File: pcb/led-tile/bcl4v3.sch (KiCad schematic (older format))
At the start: 36 parts, among them J1 Conn_01x04, J10 Conn_01x04, J2 Conn_01x04, J3 Conn_01x04, J4 Conn_01x04, J5 Conn_01x04, J6 Conn_01x04, J7 Conn_01x04, J8 Conn_01x04, J9 10118194-0001LF, Q1 IRLML6402, U1 STM32F072CBTx, U2 74HC595D_118, U3 TBD62783A, U4 TLC5916ID, U5 MCP1703A-3302_SOT23, Y1 ABS07-120-32.768KHZ-Z

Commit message: pcb: put USB_VBUS to pin header
Replace one pin header with a 5-contact version and route USB_VBUS
to this pin. Necessary to power a plug-on battery shield from the main
USB connector.
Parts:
- removed J3: Conn_01x04, Connector_PinHeader_2.54mm:PinHeader_1x04_P2.54mm_Vertical, symbol Connector_Generic:Conn_01x04
- added J4: Conn_01x05, Connector_PinHeader_2.54mm:PinHeader_1x05_P2.54mm_Vertical, symbol Connector_Generic:Conn_01x05
- LOGO1: symbol bcl4v3-rescue:OSHW-LOGOM-SparkFun-Aesthetics -> bcl4v3-rescue:OSHW-LOGOM-SparkFun-Aesthetics-bcl4v3-rescue-bcl4v3-rescue
- R4: value 680R -> 715R
- renumbered J4 to J3
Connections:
- wire segments 211 -> 212
- no-connect marks 19 -> 17
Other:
- moved on the sheet: J3
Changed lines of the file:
@@
 $Comp
 L Connector_Generic:Conn_01x04 J3
-U 1 1 5BE83443
+U 1 1 5BE834A1
 P 2550 1700
 F 0 "J3" H 2630 1692 50  0000 L CNN
-F 1 "Conn_01x04" H 2630 1601 50  0000 L CNN
+F 1 "Conn_01x04" H 2650 1600 50  0000 L CNN
 F 2 "Connector_PinHeader_2.54mm:PinHeader_1x04_P2.54mm_Vertical" H 2550 1700 50  0001 C CNN
 F 3 "~" H 2550 1700 50  0001 C CNN
 	1    2550 1700
 	1    0    0    -1
-$EndComp
-$Comp
-L Connector_Generic:Conn_01x04 J4
-U 1 1 5BE834A1
-P 2550 2400
-F 0 "J4" H 2630 2392 50  0000 L CNN
-F 1 "Conn_01x04" H 2650 2300 50  0000 L CNN
-F 2 "Connector_PinHeader_2.54mm:PinHeader_1x04_P2.54mm_Vertical" H 2550 2400 50  0001 C CNN
-F 3 "~" H 2550 2400 50  0001 C CNN
-	1    2550 2400
-	1    0    0    1
 $EndComp
 Wire Wire Line
@@
 P 7350 5950
 F 0 "R4" H 7500 6000 50  0000 C CNN
-F 1 "680R" H 7550 5900 50  0000 C CNN
+F 1 "715R" H 7550 5900 50  0000 C CNN
 F 2 "Resistor_SMD:R_0805_2012Metric_Pad1.15x1.40mm_HandSolder" V 7280 5950 50  0001 C CNN
 F 3 "~" H 7350 5950 50  0001 C CNN
@@
 NoConn ~ 4950 2000
 NoConn ~ 4950 2200
-NoConn ~ 4950 2300
-NoConn ~ 4950 2400
 NoConn ~ 4950 2600
 NoConn ~ 4950 2700
@@
 $EndComp
 $Comp
-L bcl4v3-rescue:OSHW-LOGOM-SparkFun-Aesthetics LOGO1
+L bcl4v3-rescue:OSHW-LOGOM-SparkFun-Aesthetics-bcl4v3-rescue-bcl4v3-rescue LOGO1
 U 1 1 5BFECBD9
 P 3750 4450
@@
 Text Label 5050 1150 0    50   ~ 0
 VBAT
+$Comp
+L Connector_Generic:Conn_01x05 J4
+U 1 1 5C7319EC
+P 2550 2300
+F 0 "J4" H 2630 2250 50  0000 L CNN
+F 1 "Conn_01x05" H 2630 2341 50  0000 L CNN
+F 2 "Connector_PinHeader_2.54mm:PinHeader_1x05_P2.54mm_Vertical" H 2550 2300 50  0001 C CNN
+F 3 "~" H 2550 2300 50  0001 C CNN
+	1    2550 2300
+	1    0    0    1
+$EndComp
+Wire Wire Line
+	1750 2100 2350 2100
+Text Label 1750 2100 0    50   ~ 0
+USB_VBUS
 $EndSCHEMATC

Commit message: pcb: update led-tile to latest version
move OSHW logo into a project specific library as not everyone has the
Sparkfun Libraries installed, decrease current through the SMD LED,
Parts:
- LOGO1: footprint Aesthetics:OSHW-LOGO-M -> project:OSHW-LOGO-M; symbol bcl4v3-rescue:OSHW-LOGOM-SparkFun-Aesthetics-bcl4v3-rescue-bcl4v3-rescue -> project:OSHW-LOGOM-SparkFun-Aesthetics
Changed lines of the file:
@@
 $EndComp
 $Comp
-L bcl4v3-rescue:OSHW-LOGOM-SparkFun-Aesthetics-bcl4v3-rescue-bcl4v3-rescue LOGO1
+L project:OSHW-LOGOM-SparkFun-Aesthetics LOGO1
 U 1 1 5BFECBD9
 P 3750 4450
 F 0 "LOGO1" H 3750 4700 45  0001 C CNN
 F 1 "OSHW-LOGOM" H 3750 4050 45  0001 C CNN
-F 2 "Aesthetics:OSHW-LOGO-M" H 3750 4750 20  0001 C CNN
+F 2 "project:OSHW-LOGO-M" H 3750 4750 20  0001 C CNN
 F 3 "" H 3750 4450 50  0001 C CNN
 F 4 "XXX-00000" H 4228 4385 60  0001 L CNN "Field4"

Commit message: pcb: use IS31FL3730 as matrix driver
reduce component count
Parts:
- removed R1: 1k, Resistor_SMD:R_0805_2012Metric_Pad1.15x1.40mm_HandSolder, symbol Device:R
- removed U1: STM32F072CBTx, Package_QFP:LQFP-48_7x7mm_P0.5mm, symbol MCU_ST_STM32F0:STM32F072CBTx
- removed U2: 74HC595D_118, Package_SO:TSSOP-16_4.4x5mm_P0.65mm, symbol dk_Logic-Shift-Registers:74HC595D_118
- removed U3: TBD62783A, Package_SO:SSOP-18_4.4x6.5mm_P0.65mm, symbol Transistor_Array:TBD62783A
- removed U4: TLC5916ID, Package_SO:TSSOP-16_4.4x5mm_P0.65mm, symbol dk_PMIC-LED-Drivers:TLC5916IN
- added C8: 100n, Capacitor_SMD:C_0805_2012Metric_Pad1.15x1.40mm_HandSolder, symbol Device:C_Small
- added JP2, JP3: Jumper_2_Open, project:SMT-JUMPER_2_NC_TRACE_NO-SILK, symbol Jumper:Jumper_2_Open
- added R3, R5: 4k7, Resistor_SMD:R_0805_2012Metric_Pad1.15x1.40mm_HandSolder, symbol Device:R_Small
- added R4: 100k, Resistor_SMD:R_0805_2012Metric_Pad1.15x1.40mm_HandSolder, symbol Device:R_Small
- added U2: STM32F072CBUx, Package_DFN_QFN:QFN-48-1EP_7x7mm_P0.5mm_EP5.6x5.6mm, symbol MCU_ST_STM32F0:STM32F072CBUx
- added U3: IS31FL3730-QFSL2, project:QFN-24-1EP_4x4mm_P0.5mm_EP2.6x2.6mm_ThermalVias, symbol is31fl3730-qfsl2:IS31FL3730-QFSL2
- C6: value 100n -> 1µF
- renumbered C3 to C1, C4 to C2, C5 to C3, C8 to C4, C1 to C5, J8 to J10, J5 to J3, J6 to J4, J9 to J5, J10 to J6, J3 to J7, J4 to J8, J7 to J9, R2 to R1, R4 to R2, U5 to U1
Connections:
- net labels added: MCU_SCL, MCU_SDA, MCU_SDB
- net labels removed: CAT_CLK, CAT_DATA, CAT_STROBE, nOE_COL, nOE_ROW
- wire segments 212 -> 210
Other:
- moved on the sheet: C3, C4

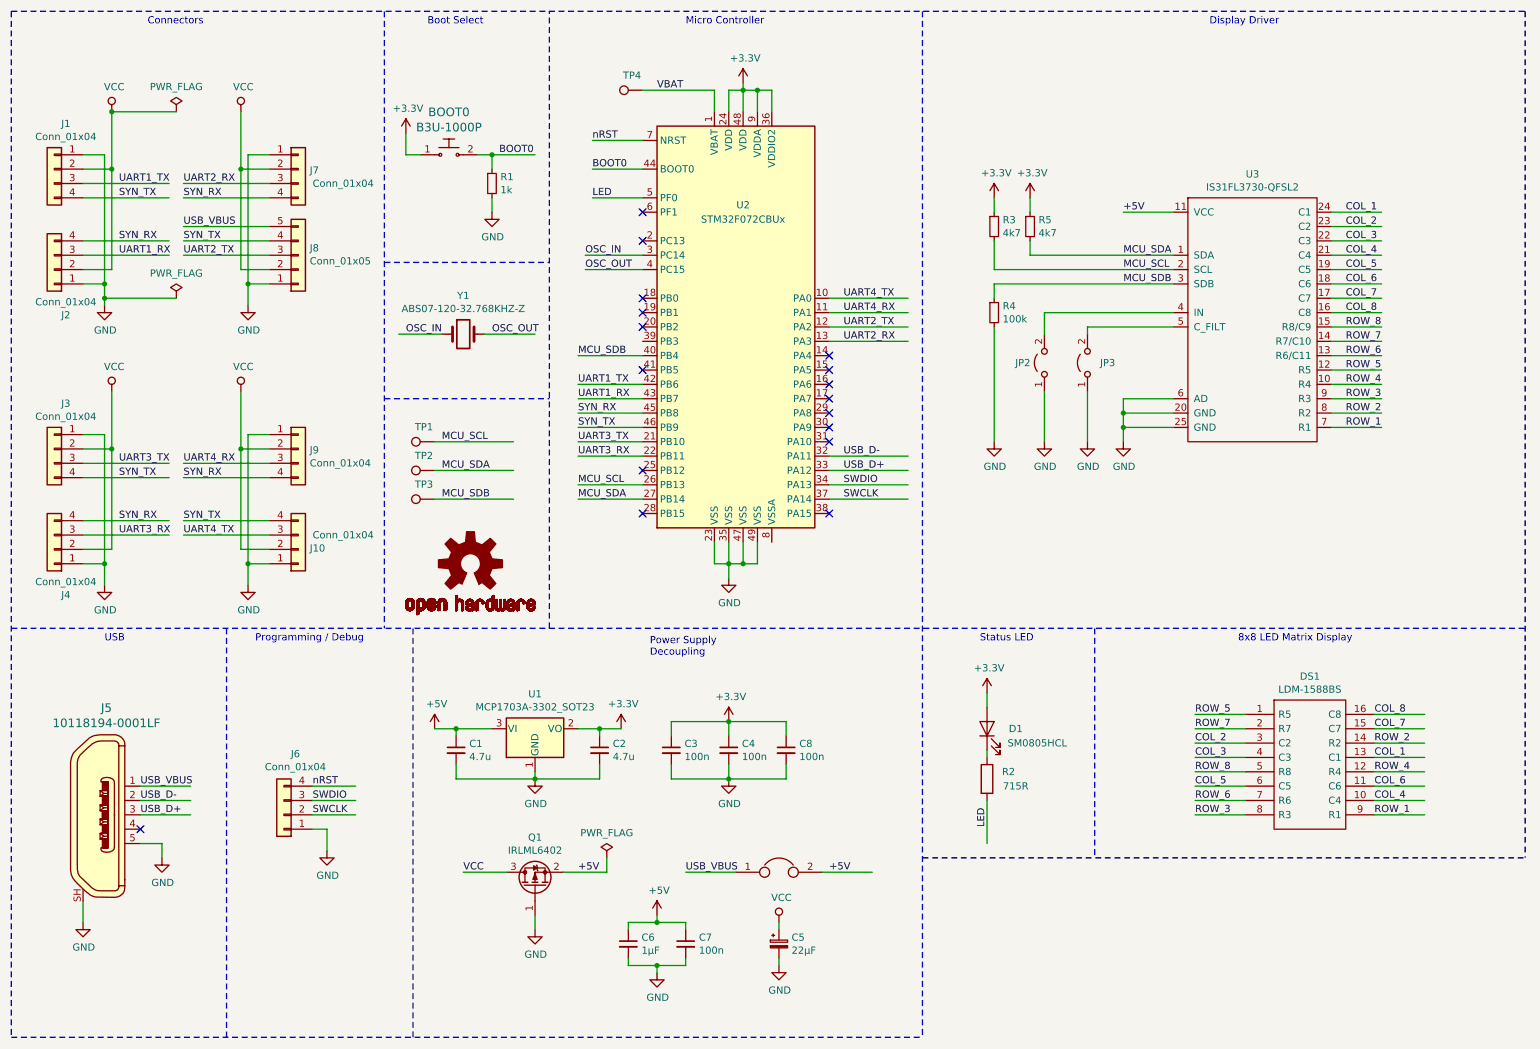
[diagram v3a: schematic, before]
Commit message: Variant of the tile with integrated LED matrix driver
Use ISSI IS31FL3736 instead of discrete ICs for driving the
LED matrix
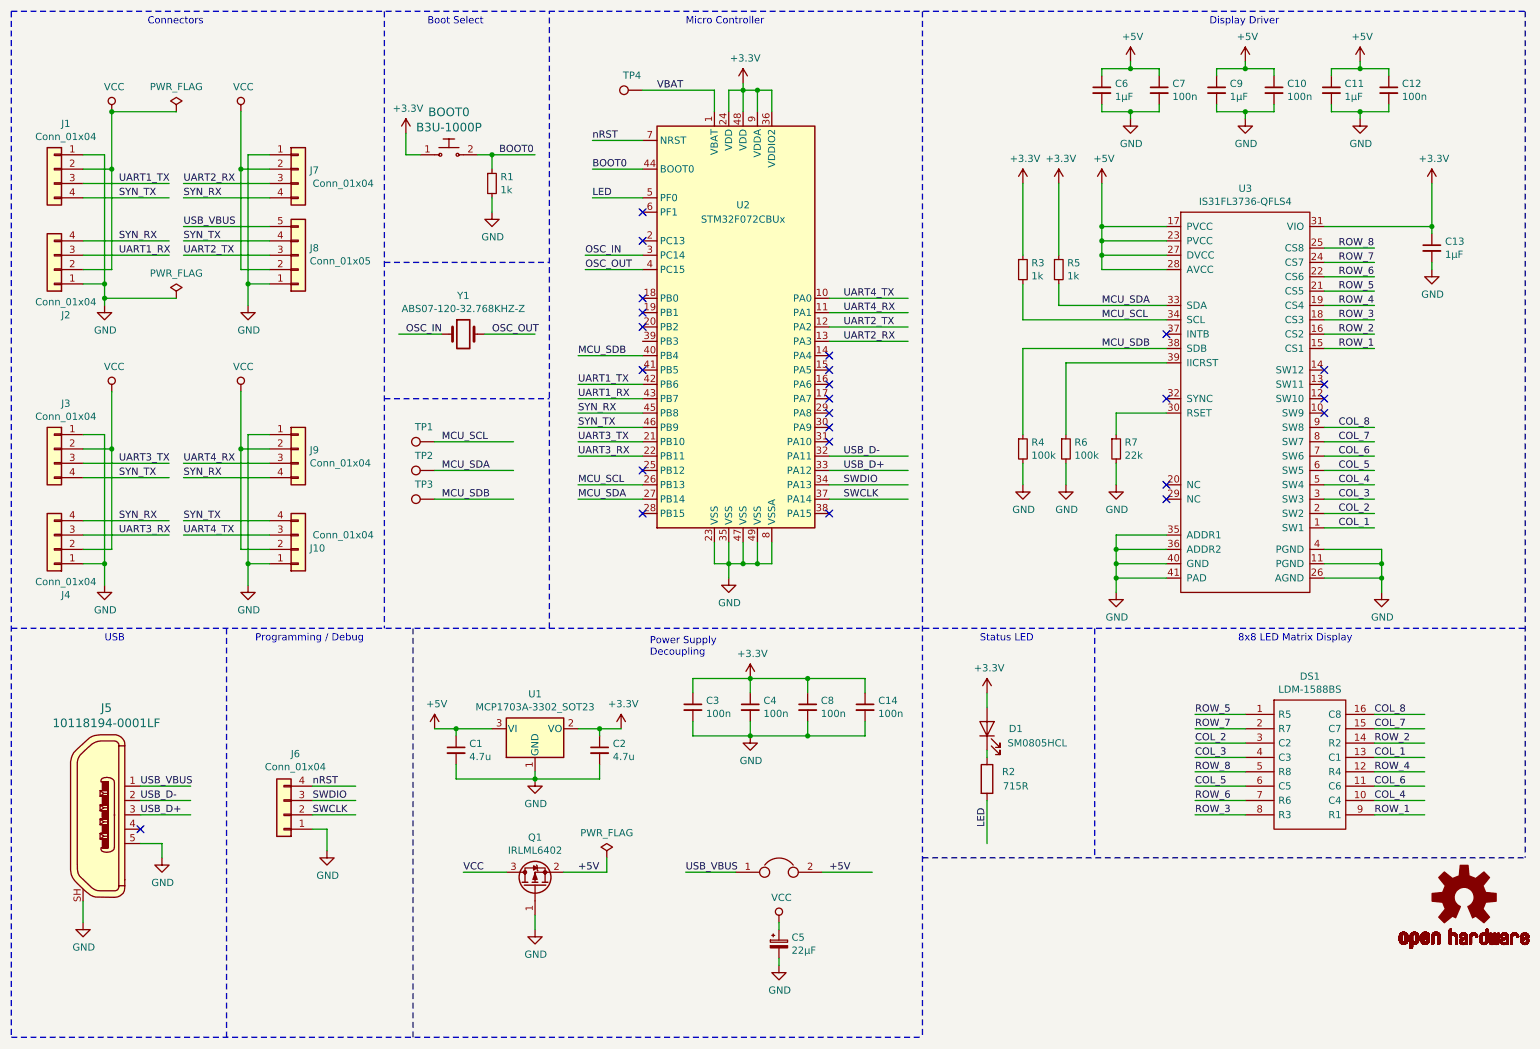
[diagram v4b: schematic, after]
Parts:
- removed JP2, JP3: Jumper_2_Open, project:SMT-JUMPER_2_NC_TRACE_NO-SILK, symbol Jumper:Jumper_2_Open
- removed U3: IS31FL3730-QFSL2, project:QFN-24-1EP_4x4mm_P0.5mm_EP2.6x2.6mm_ThermalVias, symbol is31fl3730-qfsl2:IS31FL3730-QFSL2
- added C10, C12, C14: 100n, Capacitor_SMD:C_0805_2012Metric_Pad1.15x1.40mm_HandSolder, symbol Device:C_Small
- added C11, C13, C9: 1µF, Capacitor_SMD:C_0805_2012Metric_Pad1.15x1.40mm_HandSolder, symbol Device:C_Small
- added R6: 100k, Resistor_SMD:R_0805_2012Metric_Pad1.15x1.40mm_HandSolder, symbol Device:R_Small
- added R7: 22k, Resistor_SMD:R_0805_2012Metric_Pad1.15x1.40mm_HandSolder, symbol Device:R_Small
- added U3: IS31FL3736-QFLS4, project:QFN-40_EP_5x5_Pitch0.4mm, symbol project:IS31FL3736-QFLS4
- R3, R5: value 4k7 -> 1k
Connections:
- wire segments 210 -> 255
- no-connect marks 17 -> 25
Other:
- moved on the sheet: C3, C4, C6, C7, C8, R3, R4, R5
